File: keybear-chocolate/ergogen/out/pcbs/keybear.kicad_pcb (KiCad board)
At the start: 2 copper layers, 136.9 x 95 mm, 46 parts

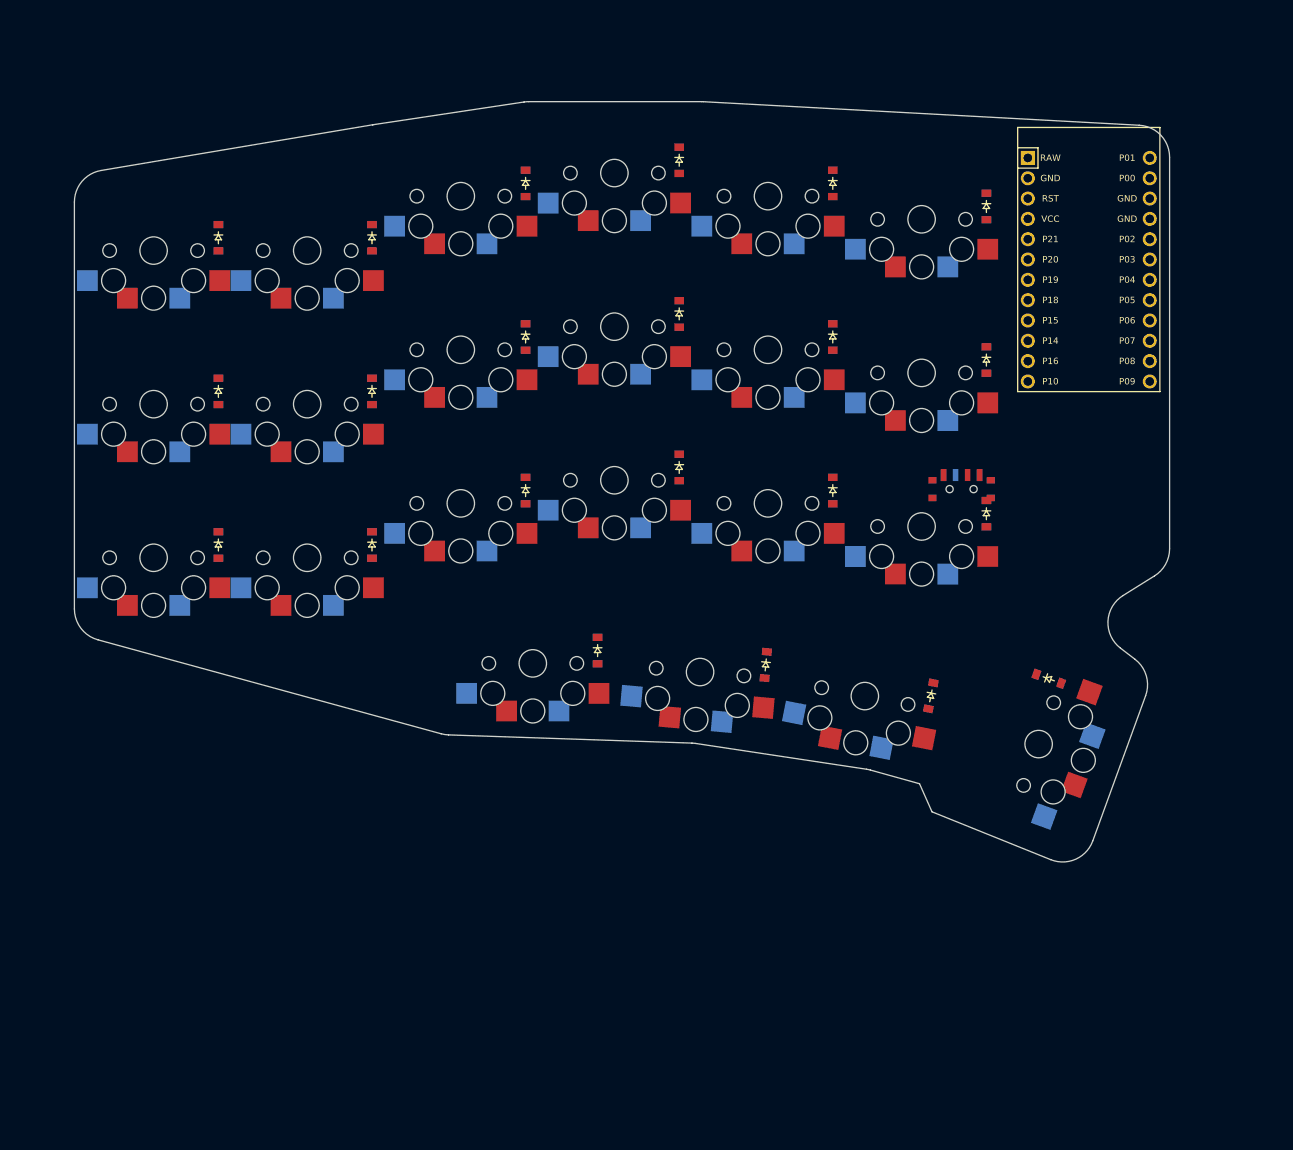
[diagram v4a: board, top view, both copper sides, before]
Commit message: changes to the pcb outline
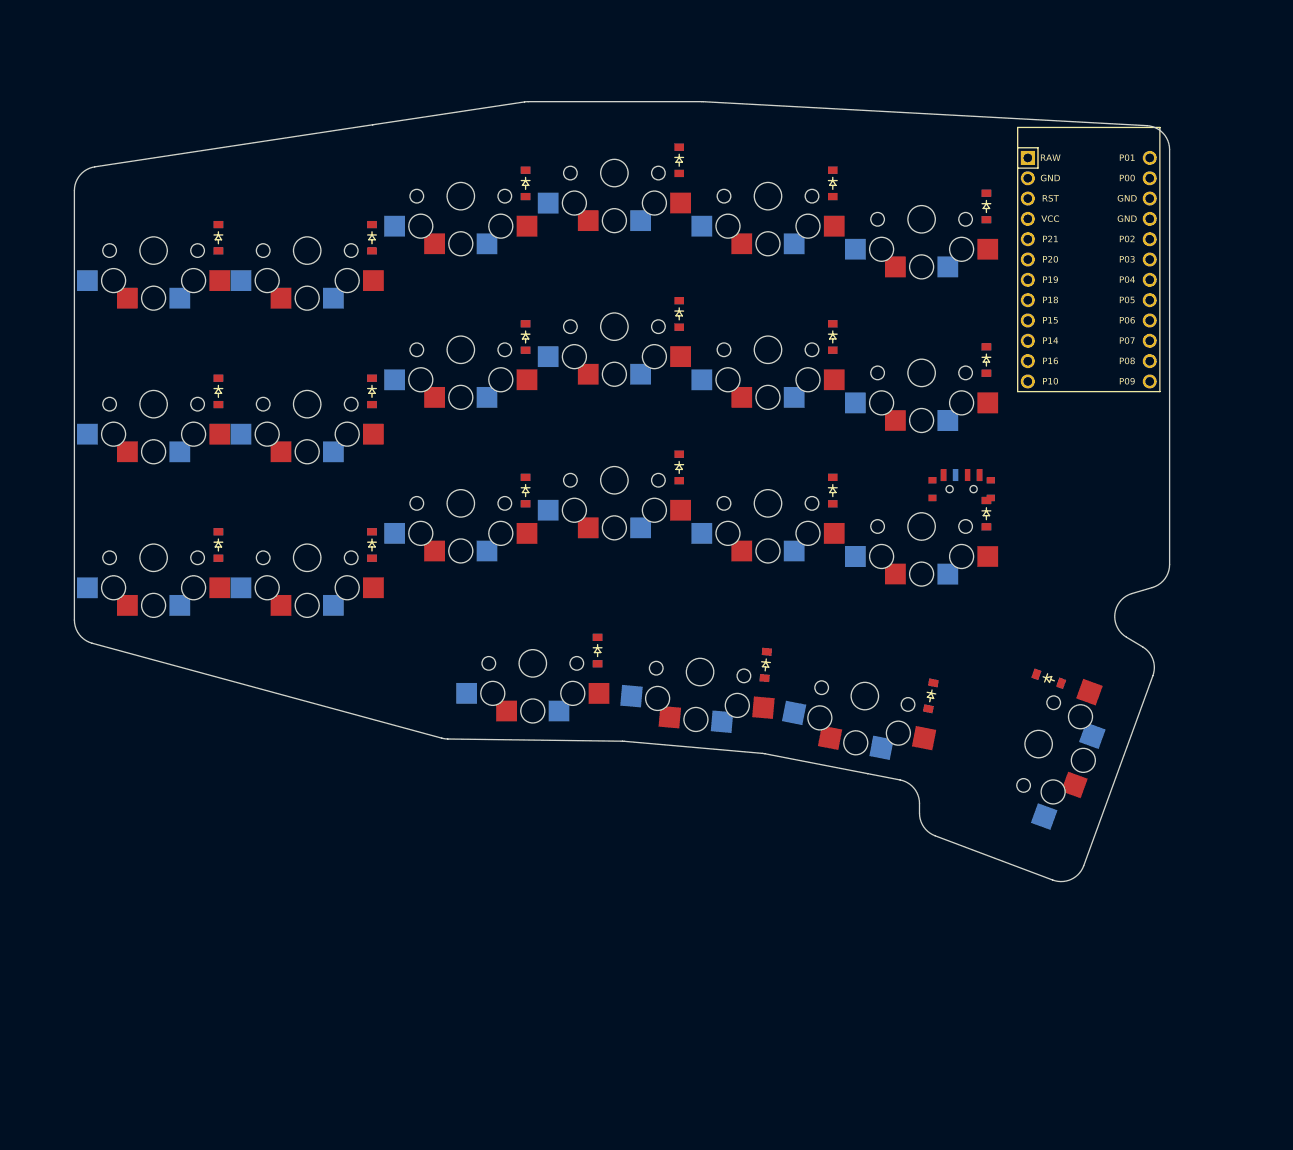
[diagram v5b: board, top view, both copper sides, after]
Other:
- board size 136.9 x 95 mm -> 136.9 x 97.5 mm
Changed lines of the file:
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@@
       (pad "" smd rect (at 3.65 -0.78) (size 1 0.8) (layers B.Cu B.Paste B.Mask))
         )
-            (gr_line (start 140.1 156.39785308660908) (end 140.1 105.5332859121984) (angle 90) (layer Edge.Cuts) (width 0.15))
-(gr_line (start 143.43640279449548 101.5887150794783) (end 177.36593794213368 95.88073027917187) (angle 90) (layer Edge.Cuts) (width 0.15))
-(gr_line (start 177.4341587601414 95.86985839495787) (end 196.3039792958942 93.02955728306591) (angle 90) (layer Edge.Cuts) (width 0.15))
-(gr_line (start 196.89935568339104 92.985) (end 218.49203019778125 92.985) (angle 90) (layer Edge.Cuts) (width 0.15))
-(gr_line (start 218.70781139778128 92.99082440000001) (end 273.21578120000004 95.93556146722602) (angle 90) (layer Edge.Cuts) (width 0.15))
-(gr_line (start 277 148.8710195142961) (end 277 99.92973706722603) (angle 90) (layer Edge.Cuts) (width 0.15))
-(gr_line (start 275.1174139550896 152.2646250423176) (end 271.1723417124503 154.72612243973228) (angle 90) (layer Edge.Cuts) (width 0.15))
-(gr_line (start 270.85763601926743 161.29538443078374) (end 272.6795398567605 162.69071421709558) (angle 90) (layer Edge.Cuts) (width 0.15))
-(gr_line (start 267.39635339320944 185.39483002577197) (end 274.00619076106904 167.2344511356605) (angle 90) (layer Edge.Cuts) (width 0.15))
-(gr_line (start 262.142513957323 187.73683977696425) (end 247.2992361 181.7553888) (angle 90) (layer Edge.Cuts) (width 0.15))
-(gr_line (start 247.2992361 181.7553888) (end 245.74070460000002 178.2434833) (angle 90) (layer Edge.Cuts) (width 0.15))
-(gr_line (start 245.74070460000002 178.2434833) (end 239.59671007807788 176.53405362901302) (angle 90) (layer Edge.Cuts) (width 0.15))
-(gr_line (start 239.12138725498585 176.43245892551334) (end 217.76099108675135 173.20906864422187) (angle 90) (layer Edge.Cuts) (width 0.15))
-(gr_line (start 217.2988866977116 173.16655802167392) (end 186.8688983707103 172.14080590472858) (angle 90) (layer Edge.Cuts) (width 0.15))
-(gr_line (start 185.94748557721738 172.00112051168963) (end 143.04382919999998 160.25589708660905) (angle 90) (layer Edge.Cuts) (width 0.15))
-(gr_arc (start 144.1 105.5332859121984) (end 143.4364028 101.5887151121984) (angle -80.45051940323589) (layer Edge.Cuts) (width 0.15))
-(gr_arc (start 178.02953514763823 99.82530111189195) (end 177.43415874763824 95.86985841189194) (angle -0.9895344017941454) (layer Edge.Cuts) (width 0.15))
-(gr_arc (start 196.89935568339104 96.985) (end 196.89935568339104 92.985) (angle -8.559946194970351) (layer Edge.Cuts) (width 0.15))
-(gr_arc (start 218.49203019778125 96.985) (end 218.70781139778126 92.9908244) (angle -3.092339062521802) (layer Edge.Cuts) (width 0.15))
-(gr_arc (start 273 99.92973706722603) (end 277 99.92973706722603) (angle -86.90766093747821) (layer Edge.Cuts) (width 0.15))
-(gr_arc (start 273 148.8710195142961) (end 275.1174139 152.26462501429612) (angle -58.0382173060583) (layer Edge.Cuts) (width 0.15))
-(gr_arc (start 273.2897556675399 158.11972796775382) (end 271.17234176753993 154.7261224677538) (angle -110.59102854572922) (layer Edge.Cuts) (width 0.15))
-(gr_arc (start 270.2474202084881 165.8663706801255) (end 274.00619070848813 167.2344510801255) (angle -72.5528093143271) (layer Edge.Cuts) (width 0.15))
-(gr_arc (start 263.6375828406285 184.02674957023692) (end 262.14251394062853 187.7368397702369) (angle -91.948141739118) (layer Edge.Cuts) (width 0.15))
-(gr_arc (start 238.52452485943897 180.38767769600435) (end 239.59671005943898 176.53405359600436) (angle -6.966571765203469) (layer Edge.Cuts) (width 0.15))
-(gr_arc (start 217.16412869120447 177.16428741471287) (end 217.76099109120446 173.20906871471288) (angle -6.650840469299183) (layer Edge.Cuts) (width 0.15))
-(gr_arc (start 187.0036563772174 168.14307651168966) (end 185.9474855772174 172.00112051168966) (angle -13.379445933893493) (layer Edge.Cuts) (width 0.15))
-(gr_arc (start 144.1 156.39785308660908) (end 140.1 156.39785308660908) (angle -74.68992248719078) (layer Edge.Cuts) (width 0.15))
+            (gr_line (start 140.1 157.78587581336933) (end 140.1 104.10013996290886) (angle 90) (layer Edge.Cuts) (width 0.15))
+(gr_line (start 142.65109021703427 101.13391677546493) (end 177.3988203601405 95.87517852726559) (angle 90) (layer Edge.Cuts) (width 0.15))
+(gr_line (start 177.4011978556094 95.87481969777545) (end 196.37798433395645 93.01841798306593) (angle 90) (layer Edge.Cuts) (width 0.15))
+(gr_line (start 196.82451662145328 92.985) (end 218.5190226483359 92.985) (angle 90) (layer Edge.Cuts) (width 0.15))
+(gr_line (start 218.68085854833595 92.9893683) (end 274.1618359 95.98667110041953) (angle 90) (layer Edge.Cuts) (width 0.15))
+(gr_line (start 277 150.84469349561692) (end 277 98.98230280041953) (angle 90) (layer Edge.Cuts) (width 0.15))
+(gr_line (start 274.8457699349969 153.7230043147176) (end 272.29609492614367 154.47220715426178) (angle 90) (layer Edge.Cuts) (width 0.15))
+(gr_line (start 271.60438377888295 159.92659094363484) (end 273.63274875310157 161.1371828691278) (angle 90) (layer Edge.Cuts) (width 0.15))
+(gr_line (start 266.26564346491665 188.5014300810883) (end 274.91434559128567 164.7393161832374) (angle 90) (layer Edge.Cuts) (width 0.15))
+(gr_line (start 262.39028563207813 190.28326447020572) (end 247.6830817080637 184.7506760037414) (angle 90) (layer Edge.Cuts) (width 0.15))
+(gr_line (start 245.73936182046077 181.9416919708019) (end 245.73980634498375 180.71740727091674) (angle 90) (layer Edge.Cuts) (width 0.15))
+(gr_line (start 243.31223354498974 177.77143637085715) (end 239.2628538056903 176.98431672743953) (angle 90) (layer Edge.Cuts) (width 0.15))
+(gr_line (start 239.26086602797358 176.98393111238738) (end 226.40528906027404 174.4940632630339) (angle 90) (layer Edge.Cuts) (width 0.15))
+(gr_line (start 226.0963169387504 174.45074636940362) (end 208.8305831062487 172.94019046402985) (angle 90) (layer Edge.Cuts) (width 0.15))
+(gr_line (start 208.6068056042486 172.92901137144023) (end 186.7808016494666 172.65478447879255) (angle 90) (layer Edge.Cuts) (width 0.15))
+(gr_line (start 186.03247292294077 172.5502199706558) (end 142.31398167471463 160.68107450650461) (angle 90) (layer Edge.Cuts) (width 0.15))
+(gr_arc (start 143.1 104.10013996290886) (end 142.6510902 101.13391676290885) (angle -81.39413273346547) (layer Edge.Cuts) (width 0.15))
+(gr_arc (start 177.84773014310622 98.84140171470952) (end 177.40119784310622 95.87481971470952) (angle -0.045921071564606564) (layer Edge.Cuts) (width 0.15))
+(gr_arc (start 196.82451662145328 95.985) (end 196.82451662145328 92.985) (angle -8.559946194970465) (layer Edge.Cuts) (width 0.15))
+(gr_arc (start 218.5190226483359 95.985) (end 218.6808585483359 92.9893683) (angle -3.0923390625223277) (layer Edge.Cuts) (width 0.15))
+(gr_arc (start 274 98.98230280041953) (end 277 98.98230280041953) (angle -86.90766093747821) (layer Edge.Cuts) (width 0.15))
+(gr_arc (start 274 150.84469349561692) (end 274.8457699 153.72300429561693) (angle -73.62497240499397) (layer Edge.Cuts) (width 0.15))
+(gr_arc (start 273.14186486114056 157.35051797336246) (end 272.29609496114057 154.47220717336245) (angle -132.7948957837653) (layer Edge.Cuts) (width 0.15))
+(gr_arc (start 272.095267670844 163.7132558394002) (end 274.91434557084403 164.73931613940022) (angle -79.16992145342795) (layer Edge.Cuts) (width 0.15))
+(gr_arc (start 263.44656554447505 187.47536973725107) (end 262.39028564447506 190.28326443725106) (angle -90.61540633540983) (layer Edge.Cuts) (width 0.15))
+(gr_arc (start 248.73936162046076 181.94278127078672) (end 245.73936182046074 181.94169197078674) (angle -69.4053996876554) (layer Edge.Cuts) (width 0.15))
+(gr_arc (start 242.73980654498374 180.71631797088776) (end 245.73980634498375 180.71740727088775) (angle -79.02080401948812) (layer Edge.Cuts) (width 0.15))
+(gr_arc (start 238.6904268056903 179.92919832743954) (end 239.2628538056903 176.98431682743953) (angle -0.03867151193470875) (layer Edge.Cuts) (width 0.15))
+(gr_arc (start 225.8348498379908 177.43933047808605) (end 226.4052890379908 174.49406327808606) (angle -5.961331016612618) (layer Edge.Cuts) (width 0.15))
+(gr_arc (start 208.56911600548904 175.92877457271223) (end 208.83058310548904 172.94019047271223) (angle -4.280160291183861) (layer Edge.Cuts) (width 0.15))
+(gr_arc (start 186.81849124822614 169.65502127752055) (end 186.03247294822614 172.55021987752053) (angle -14.469293378109853) (layer Edge.Cuts) (width 0.15))
+(gr_arc (start 143.1 157.78587581336933) (end 140.1 157.78587581336933) (angle -74.81086936254309) (layer Edge.Cuts) (width 0.15))
 )
